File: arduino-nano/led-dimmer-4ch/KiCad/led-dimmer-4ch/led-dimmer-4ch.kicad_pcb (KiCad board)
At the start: 2 copper layers, 78.7 x 66.7 mm, 45 parts, among them J1 Screw_Terminal_01x02, J2 Screw_Terminal_01x04, J3 Screw_Terminal_01x04, J4 Screw_Terminal_01x04, J5 Screw_Terminal_01x04, U1 PT4115, U2 PT4115, U3 PT4115, U4 PT4115, U5 AP63205WU

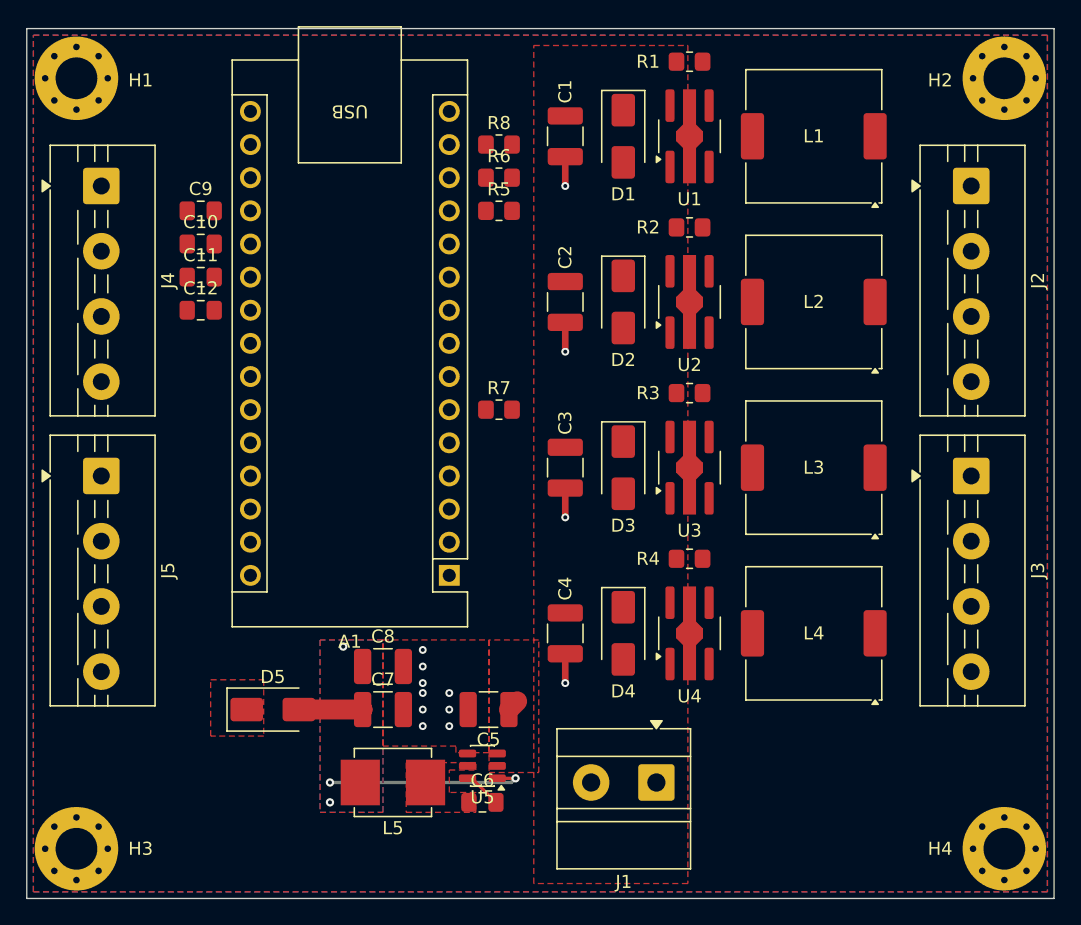
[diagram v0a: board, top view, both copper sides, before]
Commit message: refactor(led-dimmer-4ch): move terminals to Phoenix MKDS 5.08 mm and snap placement to the 25 mil grid
- What: swaps J1 to TerminalBlock_Phoenix_MKDS-1,5-2-5.08 and J2-J5 to TerminalBlock_Phoenix_MKDS-1,5-4-5.08 in the schematic and PCB, rotates the terminals to face the board edges, moves the Nano down, and snaps J1 and A1 onto the 25 mil grid.
- Why: the MaiXu and Metz 5.00 mm footprints put every pad after pin 1 off the mil grid, and the microwave already uses MKDS 5.08 mm.
- How: replaced each footprint in place keeping pin 1, nets, fields, and label positions, then refilled zones.
- Benefit: every terminal pad sits 200 mil apart on the board grid, and both boards order the same terminal part.
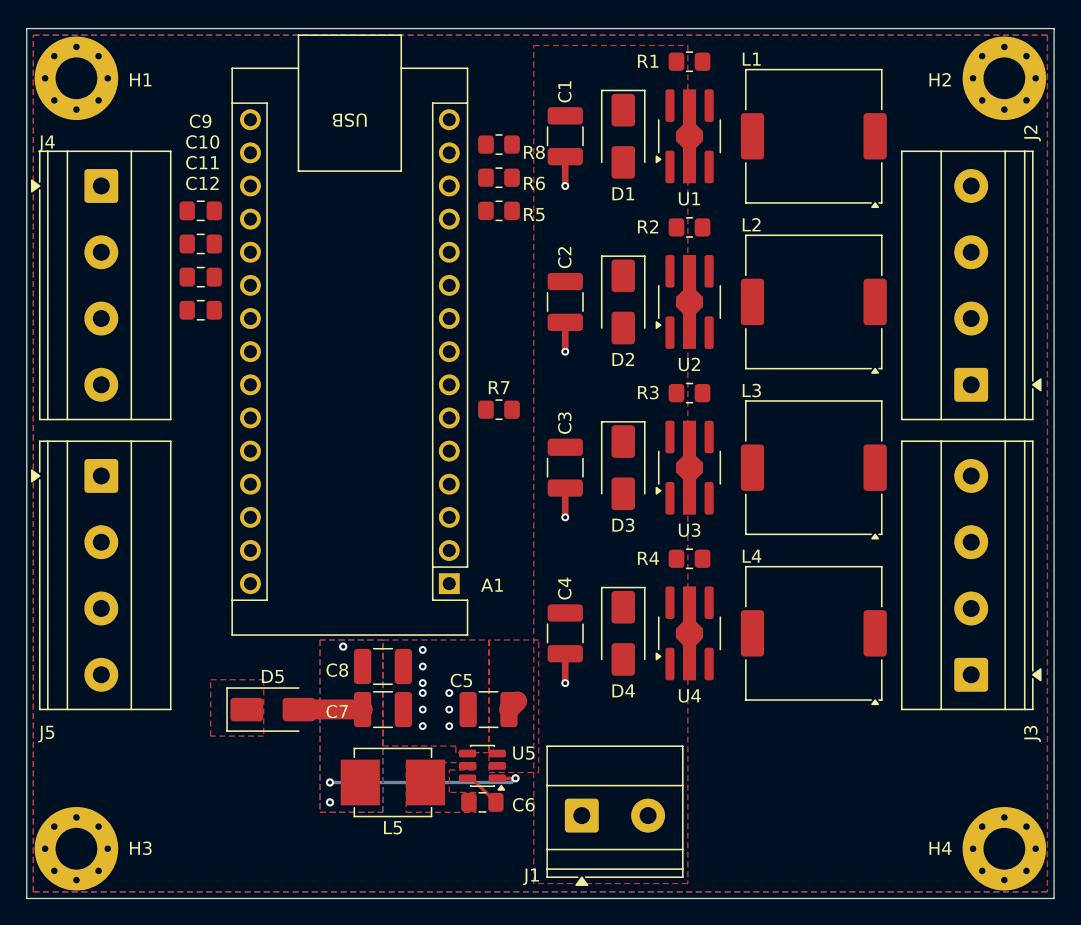
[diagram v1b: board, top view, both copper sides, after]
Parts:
- J1: footprint TerminalBlock_MetzConnect:TerminalBlock_MetzConnect_Type011_RT05502HBLC_1x02_P5.00mm_Horizontal -> TerminalBlock_Phoenix:TerminalBlock_Phoenix_MKDS-1,5-2-5.08_1x02_P5.08mm_Horizontal
- J2, J3, J4, J5: footprint TerminalBlock:TerminalBlock_MaiXu_MX126-5.0-04P_1x04_P5.00mm -> TerminalBlock_Phoenix:TerminalBlock_Phoenix_MKDS-1,5-4-5.08_1x04_P5.08mm_Horizontal
- moved J3 15.2 mm to (97.8, 74.9), turned to 90 degrees
- moved J2 15.2 mm to (97.8, 52.7), turned to 90 degrees
- moved J1 6.25 mm to (67.9, 85.7), turned to 0 degrees
- moved A1 0.63 mm to (57.8, 67.9)

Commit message: feat(led-dimmer-4ch): route the board on the mil standard with solid pours
- What: routes every net on 2 layers, reverses the J2/J3 net labels so pins 4 to 1 carry LED1+, LED1-, LED2+, LED2- (J3 the same for channels 3 and 4), adds Default (10 mil) and Power (20 mil) net classes, and sets all pours to solid pad connections.
- Why: the board had 39 unconnected pads, and rotating J2/J3 outward reversed their pin order against the driver order, so every LED pair would have crossed.
- How: SW, LED, and pot nets on F.Cu, PWM and +5V on B.Cu under the +12V strip, GND stitching vias at each PT4115 tab, inductor, filter cap, and enclosed pocket, with all tracks at 10, 20, or 60 mil and every via 24/12 mil.
- Benefit: DRC reports 0 violations and 0 unconnected pads, ERC is clean, and the firmware pin map (D9, D10, D3, D11 and A0 to A3) is unchanged.
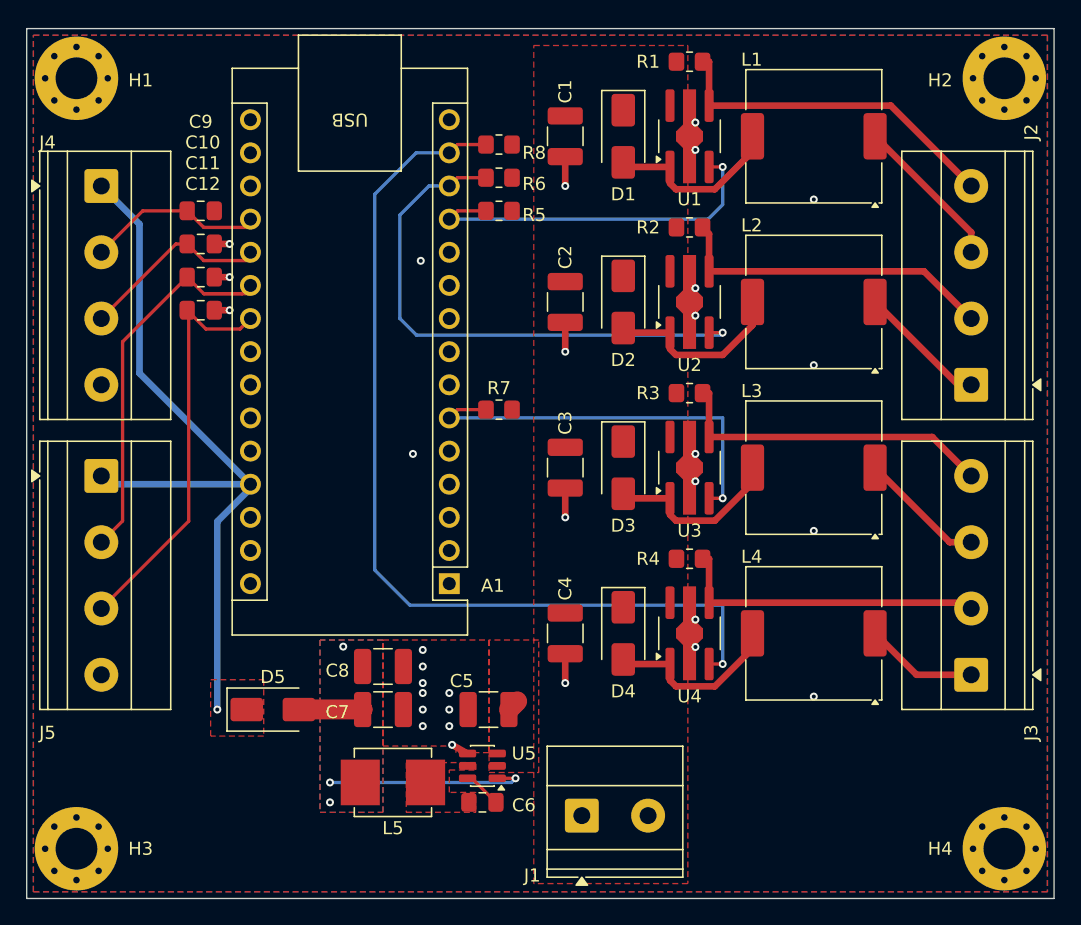
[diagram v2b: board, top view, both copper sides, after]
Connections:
- J2 pad 1: LED1+ -> LED2-
- J2 pad 2: LED1- -> LED2+
- J2 pad 3: LED2+ -> LED1-
- J2 pad 4: LED2- -> LED1+
- J3 pad 1: LED3+ -> LED4-
- J3 pad 2: LED3- -> LED4+
- J3 pad 3: LED4+ -> LED3-
- J3 pad 4: LED4- -> LED3+
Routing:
- net PWM_4: track 0.00 -> 72.2 mm, vias 0 -> 1
- net +5V: track 0.00 -> 57.6 mm, vias 0 -> 1
- net PWM_2: track 0.00 -> 42.2 mm, vias 0 -> 1
- net POT_3: track 0.00 -> 32.3 mm
- net POT_4: track 0.00 -> 31.5 mm
- net PWM_3: track 0.00 -> 31.2 mm, vias 0 -> 1
- net PWM_1: track 0.00 -> 28.4 mm, vias 0 -> 1
- net LED1+: track 0.00 -> 26.5 mm
- net LED3+: track 0.00 -> 25.2 mm
- net LED2+: track 0.00 -> 25.2 mm
- net LED4+: track 0.00 -> 24.1 mm
- net POT_2: track 0.00 -> 14.3 mm
- net Net-(D2-A): track 0.00 -> 14.1 mm
- net Net-(D4-A): track 0.00 -> 13.7 mm
- net Net-(D3-A): track 0.00 -> 13.7 mm
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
